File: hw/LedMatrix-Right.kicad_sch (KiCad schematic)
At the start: 84 parts, among them Q1400 DTA114E, Q1401 DTA114E, Q1402 DTA114E, Q1403 DTA114E, Q1404 DTA114E, Q1405 DTA114E, Q1406 DTA114E, Q1407 DTA114E, Q1408 DTA114E, Q1409 DTC114EE, Q1410 DTC114EE, Q1411 DTC114EE, Q1412 DTC114EE, Q1413 DTC114EE, Q1414 DTC114EE, Q1415 DTC114EE, Q1416 DTC114EE, Q1417 DTC114EE, Q1418 DTC114EE, Q1419 DTC114EE, Q1420 DTC114EE, Q1421 DTC114EE, Q1422 DTC114EE, Q1423 DTC114EE, X1400 Lightpipe-5x5mm-Dome, X1401 Lightpipe-5x5mm-Dome, X1402 Lightpipe-5x5mm-Dome

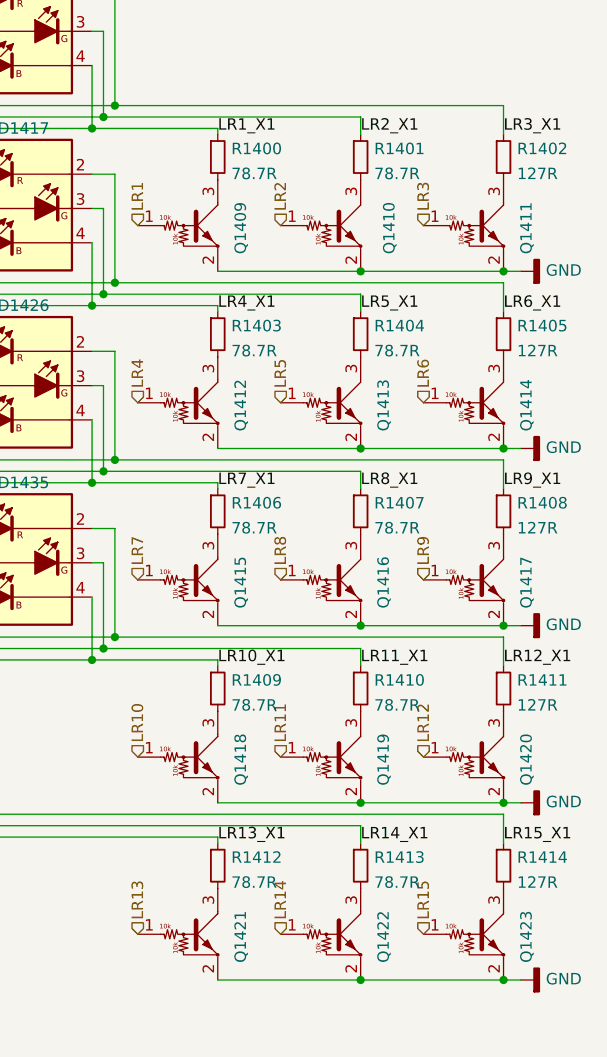
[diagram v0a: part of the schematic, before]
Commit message: Add 300R symbol and use it at green LEDs.
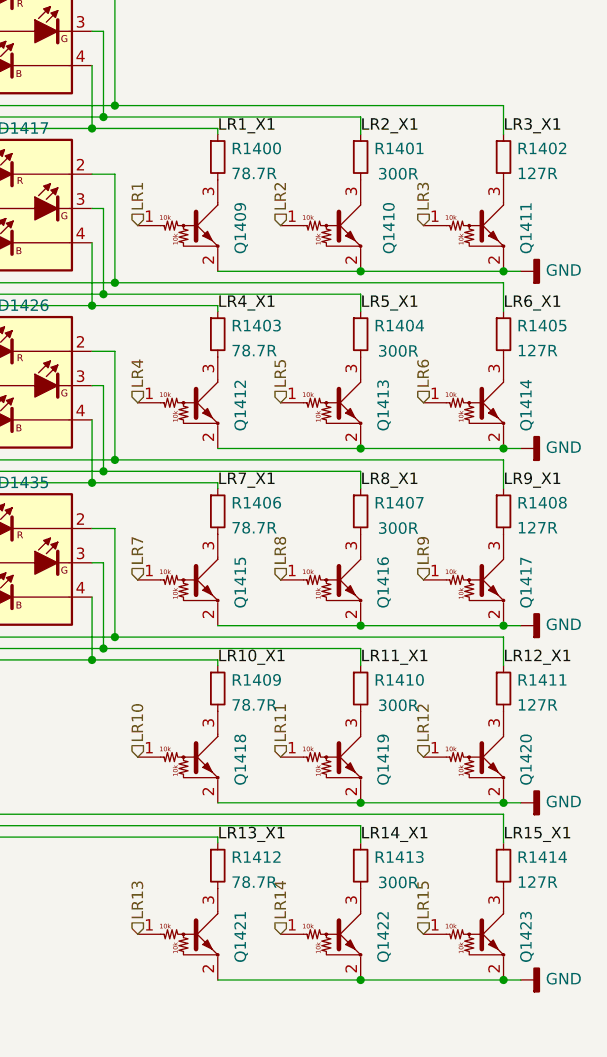
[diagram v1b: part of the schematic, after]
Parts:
- R1401, R1404, R1407, R1410, R1413: value 78.7R -> 300R; symbol Keyboard:78.7R -> Keyboard:300R; manf# RC0402FR-0778R7L -> ERJ-2RKF3000X; mouser# 603-RC0402FR-0778R7L -> 667-ERJ-2RKF3000X
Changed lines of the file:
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@@
     (pin "3")
   )
-  (symbol (lib_id "Keyboard:78.7R") (at 236.22 97.79 0) (unit 1)
-    (in_bom yes) (on_board yes) (fields_autoplaced)
+  (symbol (lib_id "Keyboard:300R") (at 236.22 97.79 0) (unit 1)
+    (in_bom yes) (on_board yes)
     (property "Reference" "R1407" (id 0) (at 237.7186 96.8815 0)
       (effects (font (size 1.27 1.27)) (justify left))
     )
-    (property "Value" "78.7R" (id 1) (at 237.7186 99.6566 0)
+    (property "Value" "300R" (id 1) (at 238.125 99.695 0)
       (effects (font (size 1.27 1.27)) (justify left))
     )
@@
       (effects (font (size 1.27 1.27)) hide)
     )
-    (property "Datasheet" "https://www.mouser.de/datasheet/2/447/PYu_RC_Group_51_RoHS_L_10-1664068.pdf" (id 3) (at 236.982 97.282 0)
-      (effects (font (size 1.27 1.27)) hide)
-    )
-    (property "mouser#" "603-RC0402FR-0778R7L" (id 4) (at 239.522 94.742 0)
-      (effects (font (size 1.524 1.524)) hide)
-    )
-    (property "manf#" "RC0402FR-0778R7L" (id 5) (at 236.22 97.79 0)
+    (property "Datasheet" "https://www.mouser.de/datasheet/2/315/AOA0000C304-1149620.pdf" (id 3) (at 236.982 97.282 0)
+      (effects (font (size 1.27 1.27)) hide)
+    )
+    (property "mouser#" "667-ERJ-2RKF3000X" (id 4) (at 239.522 94.742 0)
+      (effects (font (size 1.524 1.524)) hide)
+    )
+    (property "manf#" "ERJ-2RKF3000X " (id 5) (at 236.22 97.79 0)
       (effects (font (size 1.27 1.27)) hide)
     )
@@
     (pin "2")
   )
-  (symbol (lib_id "Keyboard:78.7R") (at 236.22 117.475 0) (unit 1)
-    (in_bom yes) (on_board yes) (fields_autoplaced)
+  (symbol (lib_id "Keyboard:300R") (at 236.22 117.475 0) (unit 1)
+    (in_bom yes) (on_board yes)
     (property "Reference" "R1410" (id 0) (at 237.7186 116.5665 0)
       (effects (font (size 1.27 1.27)) (justify left))
     )
-    (property "Value" "78.7R" (id 1) (at 237.7186 119.3416 0)
+    (property "Value" "300R" (id 1) (at 238.125 119.38 0)
       (effects (font (size 1.27 1.27)) (justify left))
     )
@@
       (effects (font (size 1.27 1.27)) hide)
     )
-    (property "Datasheet" "https://www.mouser.de/datasheet/2/447/PYu_RC_Group_51_RoHS_L_10-1664068.pdf" (id 3) (at 236.982 116.967 0)
-      (effects (font (size 1.27 1.27)) hide)
-    )
-    (property "mouser#" "603-RC0402FR-0778R7L" (id 4) (at 239.522 114.427 0)
-      (effects (font (size 1.524 1.524)) hide)
-    )
-    (property "manf#" "RC0402FR-0778R7L" (id 5) (at 236.22 117.475 0)
-      (effects (font (size 1.27 1.27)) hide)
-    )
-    (pin "1")
-    (pin "2")
-  )
-  (symbol (lib_id "Keyboard:78.7R") (at 236.22 137.16 0) (unit 1)
-    (in_bom yes) (on_board yes) (fields_autoplaced)
+    (property "Datasheet" "https://www.mouser.de/datasheet/2/315/AOA0000C304-1149620.pdf" (id 3) (at 236.982 116.967 0)
+      (effects (font (size 1.27 1.27)) hide)
+    )
+    (property "mouser#" "667-ERJ-2RKF3000X" (id 4) (at 239.522 114.427 0)
+      (effects (font (size 1.524 1.524)) hide)
+    )
+    (property "manf#" "ERJ-2RKF3000X " (id 5) (at 236.22 117.475 0)
+      (effects (font (size 1.27 1.27)) hide)
+    )
+    (pin "1")
+    (pin "2")
+  )
+  (symbol (lib_id "Keyboard:300R") (at 236.22 137.16 0) (unit 1)
+    (in_bom yes) (on_board yes)
     (property "Reference" "R1413" (id 0) (at 237.7186 136.2515 0)
       (effects (font (size 1.27 1.27)) (justify left))
     )
-    (property "Value" "78.7R" (id 1) (at 237.7186 139.0266 0)
+    (property "Value" "300R" (id 1) (at 238.125 139.065 0)
       (effects (font (size 1.27 1.27)) (justify left))
     )
@@
       (effects (font (size 1.27 1.27)) hide)
     )
-    (property "Datasheet" "https://www.mouser.de/datasheet/2/447/PYu_RC_Group_51_RoHS_L_10-1664068.pdf" (id 3) (at 236.982 136.652 0)
-      (effects (font (size 1.27 1.27)) hide)
-    )
-    (property "mouser#" "603-RC0402FR-0778R7L" (id 4) (at 239.522 134.112 0)
-      (effects (font (size 1.524 1.524)) hide)
-    )
-    (property "manf#" "RC0402FR-0778R7L" (id 5) (at 236.22 137.16 0)
-      (effects (font (size 1.27 1.27)) hide)
-    )
-    (pin "1")
-    (pin "2")
-  )
-  (symbol (lib_id "Keyboard:78.7R") (at 236.22 78.105 0) (unit 1)
-    (in_bom yes) (on_board yes) (fields_autoplaced)
+    (property "Datasheet" "https://www.mouser.de/datasheet/2/315/AOA0000C304-1149620.pdf" (id 3) (at 236.982 136.652 0)
+      (effects (font (size 1.27 1.27)) hide)
+    )
+    (property "mouser#" "667-ERJ-2RKF3000X" (id 4) (at 239.522 134.112 0)
+      (effects (font (size 1.524 1.524)) hide)
+    )
+    (property "manf#" "ERJ-2RKF3000X " (id 5) (at 236.22 137.16 0)
+      (effects (font (size 1.27 1.27)) hide)
+    )
+    (pin "1")
+    (pin "2")
+  )
+  (symbol (lib_id "Keyboard:300R") (at 236.22 78.105 0) (unit 1)
+    (in_bom yes) (on_board yes)
     (property "Reference" "R1404" (id 0) (at 237.7186 77.1965 0)
       (effects (font (size 1.27 1.27)) (justify left))
     )
-    (property "Value" "78.7R" (id 1) (at 237.7186 79.9716 0)
+    (property "Value" "300R" (id 1) (at 238.125 80.01 0)
       (effects (font (size 1.27 1.27)) (justify left))
     )
@@
       (effects (font (size 1.27 1.27)) hide)
     )
-    (property "Datasheet" "https://www.mouser.de/datasheet/2/447/PYu_RC_Group_51_RoHS_L_10-1664068.pdf" (id 3) (at 236.982 77.597 0)
-      (effects (font (size 1.27 1.27)) hide)
-    )
-    (property "mouser#" "603-RC0402FR-0778R7L" (id 4) (at 239.522 75.057 0)
-      (effects (font (size 1.524 1.524)) hide)
-    )
-    (property "manf#" "RC0402FR-0778R7L" (id 5) (at 236.22 78.105 0)
+    (property "Datasheet" "https://www.mouser.de/datasheet/2/315/AOA0000C304-1149620.pdf" (id 3) (at 236.982 77.597 0)
+      (effects (font (size 1.27 1.27)) hide)
+    )
+    (property "mouser#" "667-ERJ-2RKF3000X" (id 4) (at 239.522 75.057 0)
+      (effects (font (size 1.524 1.524)) hide)
+    )
+    (property "manf#" "ERJ-2RKF3000X " (id 5) (at 236.22 78.105 0)
       (effects (font (size 1.27 1.27)) hide)
     )
@@
     (pin "2")
   )
-  (symbol (lib_id "Keyboard:78.7R") (at 236.22 58.42 0) (unit 1)
-    (in_bom yes) (on_board yes) (fields_autoplaced)
+  (symbol (lib_id "Keyboard:300R") (at 236.22 58.42 0) (unit 1)
+    (in_bom yes) (on_board yes)
     (property "Reference" "R1401" (id 0) (at 237.7186 57.5115 0)
       (effects (font (size 1.27 1.27)) (justify left))
     )
-    (property "Value" "78.7R" (id 1) (at 237.7186 60.2866 0)
+    (property "Value" "300R" (id 1) (at 238.125 60.325 0)
       (effects (font (size 1.27 1.27)) (justify left))
     )
@@
       (effects (font (size 1.27 1.27)) hide)
     )
-    (property "Datasheet" "https://www.mouser.de/datasheet/2/447/PYu_RC_Group_51_RoHS_L_10-1664068.pdf" (id 3) (at 236.982 57.912 0)
-      (effects (font (size 1.27 1.27)) hide)
-    )
-    (property "mouser#" "603-RC0402FR-0778R7L" (id 4) (at 239.522 55.372 0)
-      (effects (font (size 1.524 1.524)) hide)
-    )
-    (property "manf#" "RC0402FR-0778R7L" (id 5) (at 236.22 58.42 0)
-      (effects (font (size 1.27 1.27)) hide)
-    )
+    (property "Datasheet" "https://www.mouser.de/datasheet/2/315/AOA0000C304-1149620.pdf" (id 3) (at 236.982 57.912 0)
+      (effects (font (size 1.27 1.27)) hide)
+    )
+    (property "mouser#" "667-ERJ-2RKF3000X" (id 4) (at 239.522 55.372 0)
+      (effects (font (size 1.524 1.524)) hide)
+    )
+    (property "manf#" "ERJ-2RKF3000X " (id 5) (at 236.22 58.42 0)
+      (effects (font (size 1.27 1.27)) hide)
+    )
